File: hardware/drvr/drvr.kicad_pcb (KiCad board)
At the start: 2 copper layers, 31 x 46 mm, 42 parts, among them J101 PinHeader2x2, J102 PinHeader2x2, J103 PinHeader2x2, J104 PinHeader2x2, J105 PinHeader2x2, J106 PinHeader2x2, U201 INA241A5xDDF, U301 INA241A5xDDF, U401 INA241A5xDDF

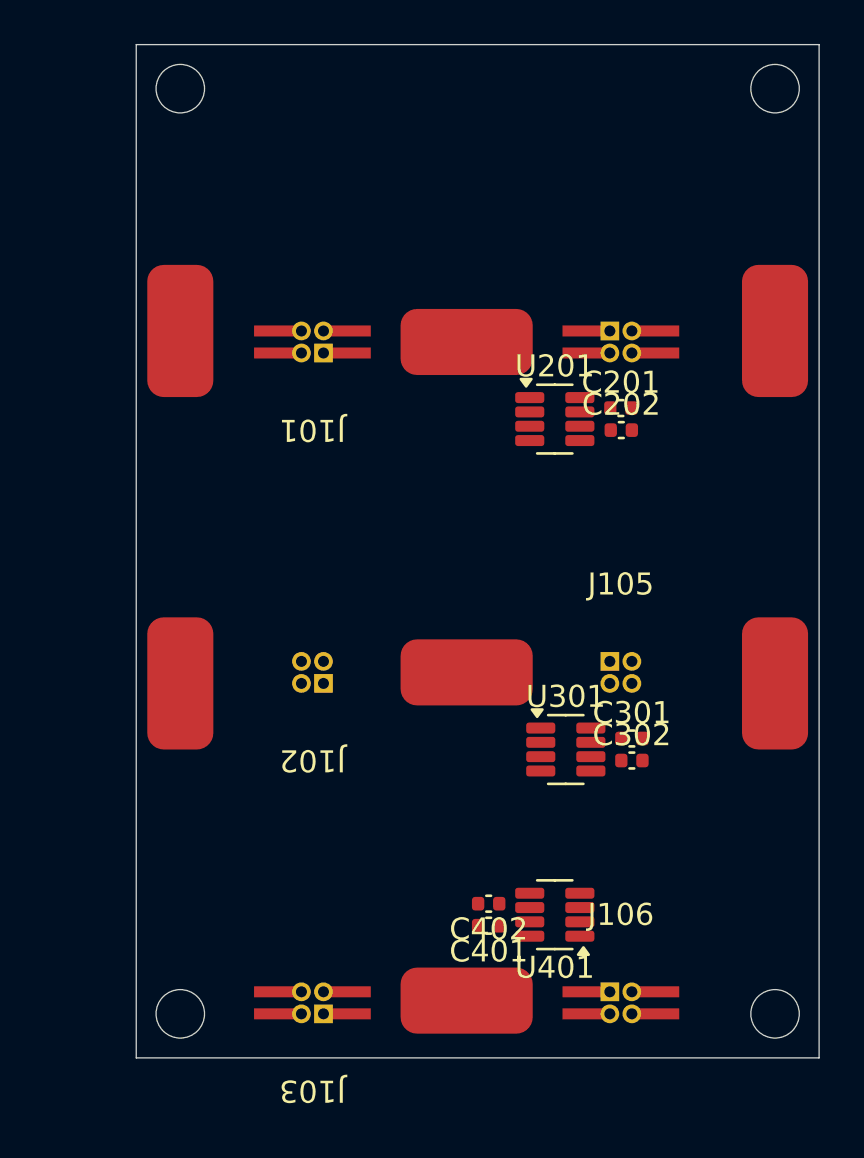
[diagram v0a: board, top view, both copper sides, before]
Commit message: added solder targets, expanded project structure
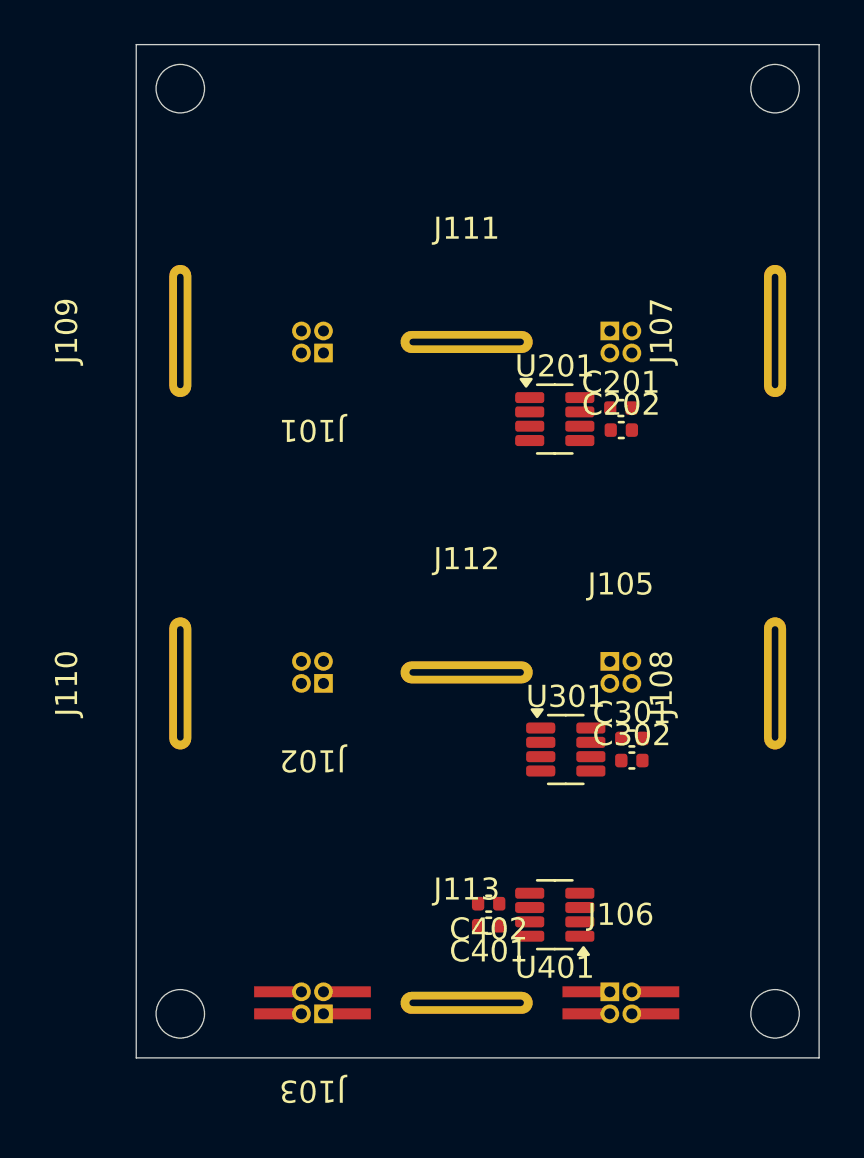
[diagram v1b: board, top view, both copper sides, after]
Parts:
- removed the ? at (157.3, 69.0)
- removed the ? at (160.7, 69.0)
- removed the ? at (166.0, 69.5)
- removed the ? at (160.7, 70.0)
- removed the ? at (180.0, 85.0)
- removed the ? at (171.3, 69.0)
- removed the ? at (174.7, 69.0)
- removed the ? at (180.0, 69.0)
- removed the ? at (157.3, 70.0)
- removed the ? at (153.0, 85.0)
- removed the ? at (166.0, 99.4)
- removed the ? at (171.3, 70.0)
- removed the ? at (166.0, 84.5)
- removed the ? at (174.7, 70.0)
- removed the ? at (153.0, 69.0)
- added J107: pwrCon_Solder_5mm, mcrmv:0.1x5mm_Strip_Cutout, F.Cu at (180.0, 69.0)
- added J108: pwrCon_Solder_5mm, mcrmv:0.1x5mm_Strip_Cutout, F.Cu at (180.0, 85.0)
- added J109: pwrCon_Solder_5mm, mcrmv:0.1x5mm_Strip_Cutout, F.Cu at (153.0, 69.0)
- added J110: pwrCon_Solder_5mm, mcrmv:0.1x5mm_Strip_Cutout, F.Cu at (153.0, 85.0)
- added J111: pwrCon_Solder_5mm, mcrmv:0.1x5mm_Strip_Cutout, F.Cu at (166.0, 69.5)
- added J112: pwrCon_Solder_5mm, mcrmv:0.1x5mm_Strip_Cutout, F.Cu at (166.0, 84.5)
- added J113: pwrCon_Solder_5mm, mcrmv:0.1x5mm_Strip_Cutout, F.Cu at (166.0, 99.5)
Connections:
- net /amp0/OUT renamed /I_P1
- net /amp1/OUT renamed /I_P2
- net /amp2/OUT renamed /I_P3

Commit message: added initial gate-drive design
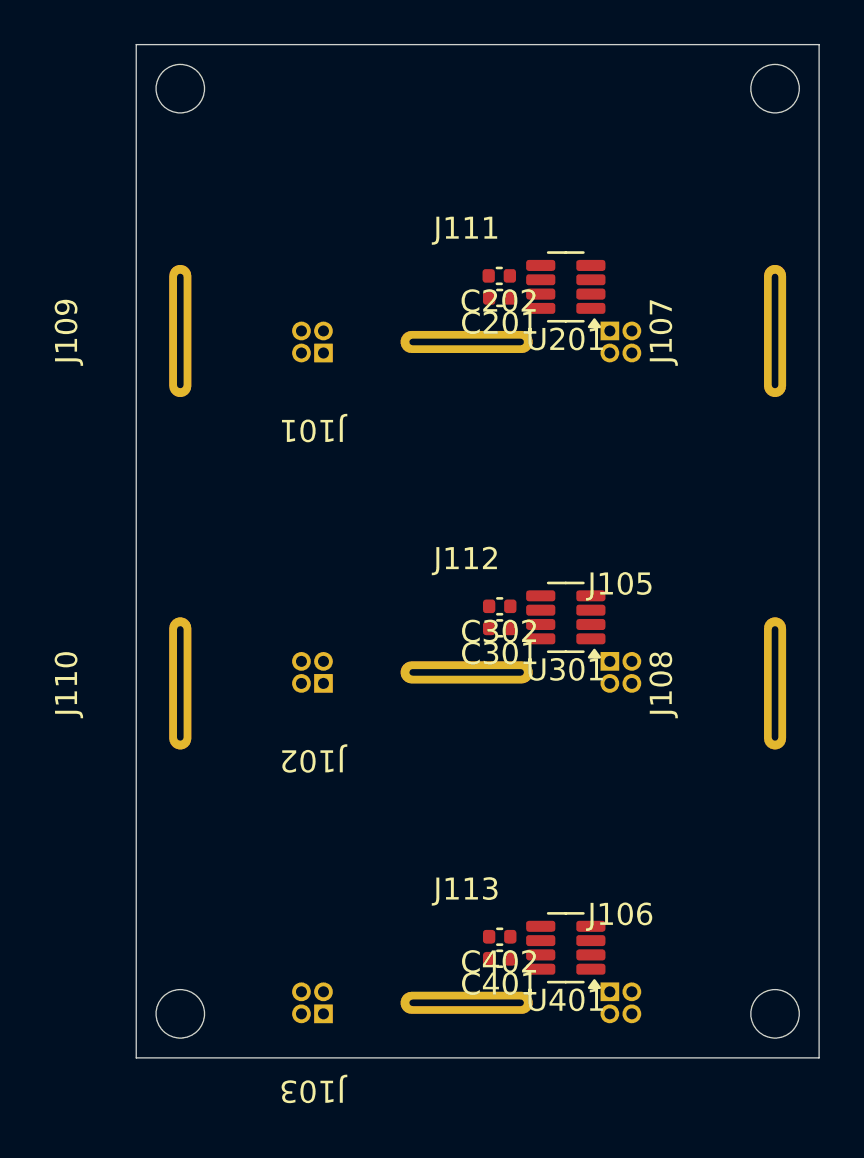
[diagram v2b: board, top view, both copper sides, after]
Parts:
- removed the ? at (157.3, 100.0)
- removed the ? at (160.7, 100.0)
- removed the ? at (157.3, 99.0)
- removed the ? at (171.3, 99.0)
- removed the ? at (171.3, 100.0)
- removed the ? at (160.7, 99.0)
- removed the ? at (174.7, 99.0)
- removed the ? at (174.7, 100.0)
- moved C302 9.22 mm to (167.5, 81.5), turned to 180 degrees
- moved C202 8.93 mm to (167.5, 66.5), turned to 180 degrees
- moved C301 7.81 mm to (167.5, 82.5), turned to 180 degrees
- moved C201 7.43 mm to (167.5, 67.5), turned to 180 degrees
- moved U201 6.02 mm to (170.5, 67.0), turned to 180 degrees
- moved U301 6.00 mm to (170.5, 82.0), turned to 180 degrees
- moved C401 1.58 mm to (167.5, 97.5)
- moved C402 1.58 mm to (167.5, 96.5)
- moved U401 1.58 mm to (170.5, 97.0)

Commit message: added gatedrivers + pico as draft
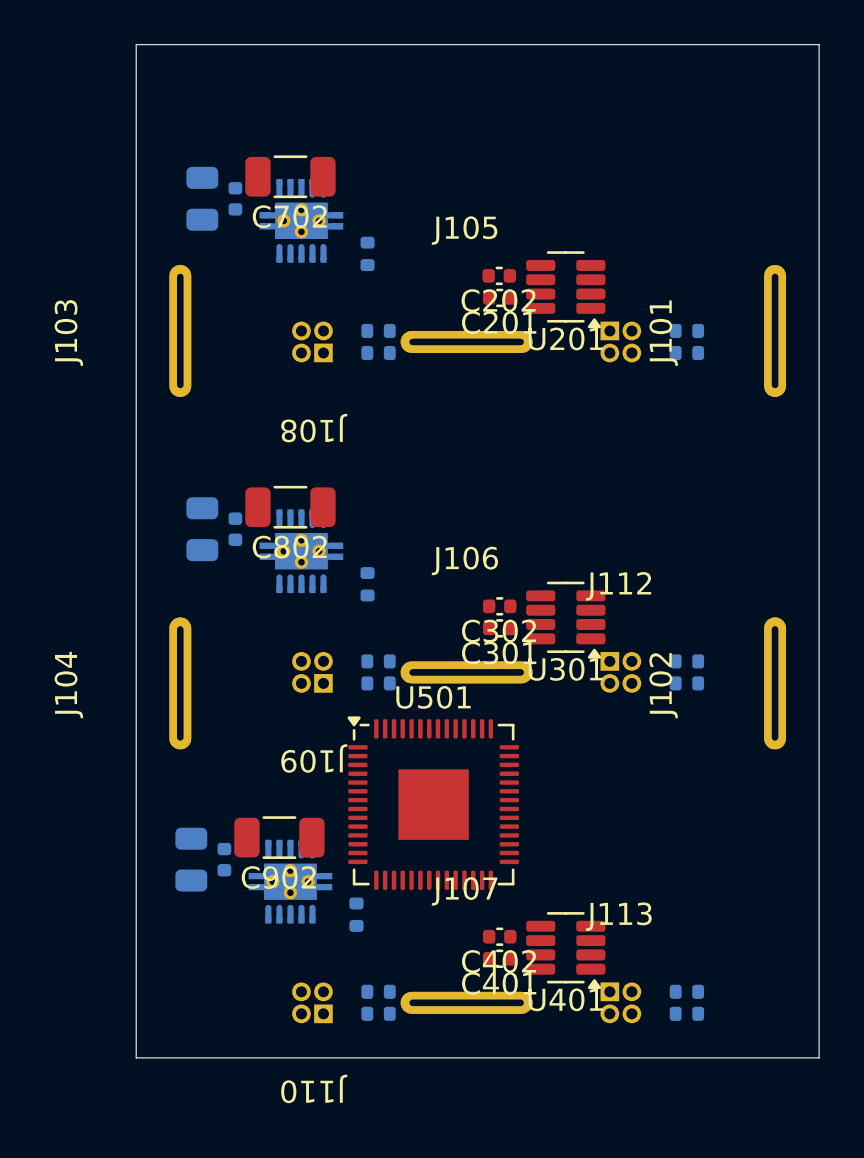
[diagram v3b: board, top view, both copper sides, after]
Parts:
- removed ? (x4): , 
- added C701: 2.2uF, Capacitor_SMD:C_0805_2012Metric, B.Cu at (154.0, 63.0)
- added C702: 0.1uF, Capacitor_SMD:C_1206_3216Metric, F.Cu at (158.0, 62.0)
- added C703: 0.1uF, Capacitor_SMD:C_0402_1005Metric, B.Cu at (155.5, 63.0)
- added C801: 2.2uF, Capacitor_SMD:C_0805_2012Metric, B.Cu at (154.0, 78.0)
- added C802: 0.1uF, Capacitor_SMD:C_1206_3216Metric, F.Cu at (158.0, 77.0)
- added C803: 0.1uF, Capacitor_SMD:C_0402_1005Metric, B.Cu at (155.5, 78.0)
- added C901: 2.2uF, Capacitor_SMD:C_0805_2012Metric, B.Cu at (153.5, 93.0)
- added C902: 0.1uF, Capacitor_SMD:C_1206_3216Metric, F.Cu at (157.5, 92.0)
- added C903: 0.1uF, Capacitor_SMD:C_0402_1005Metric, B.Cu at (155.0, 93.0)
- added R101: 10, Resistor_SMD:R_0402_1005Metric, B.Cu at (176.0, 70.0)
- added R102: 10, Resistor_SMD:R_0402_1005Metric, B.Cu at (176.0, 85.0)
- added R103: 10, Resistor_SMD:R_0402_1005Metric, B.Cu at (176.0, 100.0)
- added R104: 10, Resistor_SMD:R_0402_1005Metric, B.Cu at (162.0, 69.0)
- added R105: 10, Resistor_SMD:R_0402_1005Metric, B.Cu at (162.0, 84.0)
- added R106: 10, Resistor_SMD:R_0402_1005Metric, B.Cu at (162.0, 99.0)
- added R107: 10, Resistor_SMD:R_0402_1005Metric, B.Cu at (176.0, 69.0)
- added R108: 10, Resistor_SMD:R_0402_1005Metric, B.Cu at (176.0, 84.0)
- added R109: 10, Resistor_SMD:R_0402_1005Metric, B.Cu at (176.0, 99.0)
- added R110: 10, Resistor_SMD:R_0402_1005Metric, B.Cu at (162.0, 70.0)
- added R111: 10, Resistor_SMD:R_0402_1005Metric, B.Cu at (162.0, 85.0)
- added R112: 10, Resistor_SMD:R_0402_1005Metric, B.Cu at (162.0, 100.0)
- added R701: 10k, Resistor_SMD:R_0402_1005Metric, B.Cu at (161.5, 65.5)
- added R801: 10k, Resistor_SMD:R_0402_1005Metric, B.Cu at (161.5, 80.5)
- added R901: 10k, Resistor_SMD:R_0402_1005Metric, B.Cu at (161.0, 95.5)
- added U501: RP2040, Package_DFN_QFN:QFN-56-1EP_7x7mm_P0.4mm_EP3.2x3.2mm, F.Cu at (164.5, 90.5)
- added U701: UCC27302A, mcrmv:DRC0010J-VSON-10, B.Cu at (158.5, 64.0)
- added U801: UCC27302A, mcrmv:DRC0010J-VSON-10, B.Cu at (158.5, 79.0)
- added U901: UCC27302A, mcrmv:DRC0010J-VSON-10, B.Cu at (158.0, 94.0)
- renumbered J107 to J101, J108 to J102, J109 to J103, J110 to J104, J111 to J105, J112 to J106, J113 to J107, J101 to J108, J102 to J109, J103 to J110, J104 to J111, J105 to J112, J106 to J113
